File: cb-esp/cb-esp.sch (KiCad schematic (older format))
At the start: 21 parts, among them P1 CONN_01X07, P2 CONN_01X07, P3 CONN_01X02, SW1 SW_PUSH_SMALL, SW2 SW_PUSH_SMALL, U1 MCP1702, U2 ESP-12E, U3 LY-SK10

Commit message: Small changes
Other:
- moved on the sheet: R3
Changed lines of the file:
@@
 L R R3
 U 1 1 5671ECCD
-P 8750 3150
-F 0 "R3" V 8830 3150 50  0000 C CNN
-F 1 "10k" V 8750 3150 50  0000 C CNN
-F 2 "mysmd:SM0603S" H 8750 3150 60  0001 C CNN
-F 3 "" H 8750 3150 60  0001 C CNN
-	1    8750 3150
+P 8800 3300
+F 0 "R3" V 8880 3300 50  0000 C CNN
+F 1 "10k" V 8800 3300 50  0000 C CNN
+F 2 "mysmd:SM0603S" H 8800 3300 60  0001 C CNN
+F 3 "" H 8800 3300 60  0001 C CNN
+	1    8800 3300
 	-1   0    0    1
 $EndComp
 Wire Wire Line
-	8750 2950 8750 3000
+	8800 2950 8800 3150
 $Comp
 L GND #PWR07
 U 1 1 5671ECD5
-P 8750 3350
-F 0 "#PWR07" H 8750 3350 30  0001 C CNN
-F 1 "GND" H 8750 3280 30  0001 C CNN
-F 2 "" H 8750 3350 60  0001 C CNN
-F 3 "" H 8750 3350 60  0001 C CNN
-	1    8750 3350
+P 8800 3500
+F 0 "#PWR07" H 8800 3500 30  0001 C CNN
+F 1 "GND" H 8800 3430 30  0001 C CNN
+F 2 "" H 8800 3500 60  0001 C CNN
+F 3 "" H 8800 3500 60  0001 C CNN
+	1    8800 3500
 	1    0    0    -1
 $EndComp
 Wire Wire Line
-	8750 3300 8750 3350
+	8800 3450 8800 3500
 NoConn ~ 7050 3550
 NoConn ~ 7150 3550
@@
 $EndComp
 Wire Wire Line
-	8750 2950 8200 2950
+	8200 2950 8800 2950
 Wire Wire Line
 	6400 2350 6050 2350

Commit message: Attaching GPIO15 to panStamp's RESET line
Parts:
- PS1: symbol PANSTAMP_NRG2 -> PANSTAMP_NRG2-RESCUE-cb-esp
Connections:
- net PS_RESET is gone; now on net GPIO15: P1.4 (P4), PS1.12 (RESET)
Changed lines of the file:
@@
 EESchema Schematic File Version 2
+LIBS:cb-esp-rescue
 LIBS:power
 LIBS:digi
@@
 Sheet 1 1
 Title "Carrier board for panStamp and ESP-12E"
-Date "2015-12-18"
+Date "2016-02-05"
 Rev "1.0"
 Comp "www.panstamp.com"
@@
 	6850 5400 7300 5400
 Wire Wire Line
-	6850 5300 7300 5300
+	6850 5300 7600 5300
 Wire Wire Line
 	6850 5600 7250 5600
@@
 	6850 5500 6950 5500
 $Comp
-L PANSTAMP_NRG2 PS1
+L PANSTAMP_NRG2-RESCUE-cb-esp PS1
 U 1 1 55D4CB6C
 P 3250 2750
@@
 $EndComp
 Wire Wire Line
-	8350 5200 7900 5200
+	7600 5200 8350 5200
 Text Label 7900 5200 0    60   ~ 0
 GPIO15
@@
 Wire Wire Line
 	8200 2550 9400 2550
+Wire Wire Line
+	7600 5300 7600 5200
 $EndSCHEMATC

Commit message: Version 1.0 released
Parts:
- removed ANT1: ANTENNA, myconnectors:SMA_RightAngle_Tyco, symbol ANTENNA
- removed P1, P2: CONN_01X07, Pin_Headers:Pin_Header_Straight_1x07, symbol CONN_01X07
- removed PS1: PANSTAMP_NRG2, mysmd:PANSTAMP_2, symbol PANSTAMP_NRG2-RESCUE-cb-esp
- removed U3: LY-SK10, mysmd:LY-SK10, symbol LY-SK10
- added D3: D_Schottky_x2_ACom_KKA, mysmd:SOT23, symbol D_Schottky_x2_ACom_KKA
- added D4: BAS16, SOD323, symbol D
- added P1: CONN_01X02, Pin_Headers:Pin_Header_Straight_1x02, symbol CONN_01X02
- added PS1: PANSTAMP_NRG2, mysmd:PANSTAMP_2, symbol PANSTAMP_NRG2
- added PS2: PANSTAMP_MINIBAT, mymods:minibat, symbol PANSTAMP_MINIBAT
- added U3: ANTENNA, myconnectors:SMA_RightAngle_Tyco, symbol ANTENNA
- added U4: LY-SK10, LY-SK10, symbol LY-SK10
- P3: footprint Pin_Headers:Pin_Header_Straight_1x02 -> myconnectors:PWR_3A
- U2: footprint mysmd:ESP-12E -> ESP8266:ESP-12E
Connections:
- net ESP_RXD: now also U4.2
- net ESP_TXD: now also U4.5
- net GND: now also SW1.2, D3.3 (A), P1.2 (P2), PS1.14 (GND), PS1.28 (GND), PS1.29 (GND), PS1.30 (GND), PS1.32 (GND), PS1.33 (GND), PS1.34 (GND), PS2.14 (GND), PS2.16 (GND), U3.2 (GND); no longer SW1.1
- net GPIO0: now also SW1.1; no longer SW1.2
- net GPIO15: now also PS1.12 (RESET), PS2.18 (RESET)
- net PS_RXD: now also PS1.17 (D5/P1.5/UART_RX), PS2.21 (D5/P1.5/UART_RX), U4.6
- net PS_TEST: now also PS1.11 (TEST), PS2.17 (TEST)
- net PS_TXD: now also PS1.16 (D6/P1.6/UART_TX), PS2.20 (D6/P1.6/UART_TX), U4.1
- net VCC: now also PS1.13 (VCC), PS2.15 (VCC)
- net at C1.1, U1.3 (Vin): now also D4.1 (K); no longer P3.1 (P1)
- new net: PS1.31 (ANTENNA), U3.1 (RF)
- new net +5V: D3.1 (K), D3.2 (K), D4.2 (A), P1.1 (P1), P3.1 (P1)
- no-connect marks 36 -> 56
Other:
- moved on the sheet: C1, C2, C3, C4, D1, D2, P3, R1, R2, R3, R4, R5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

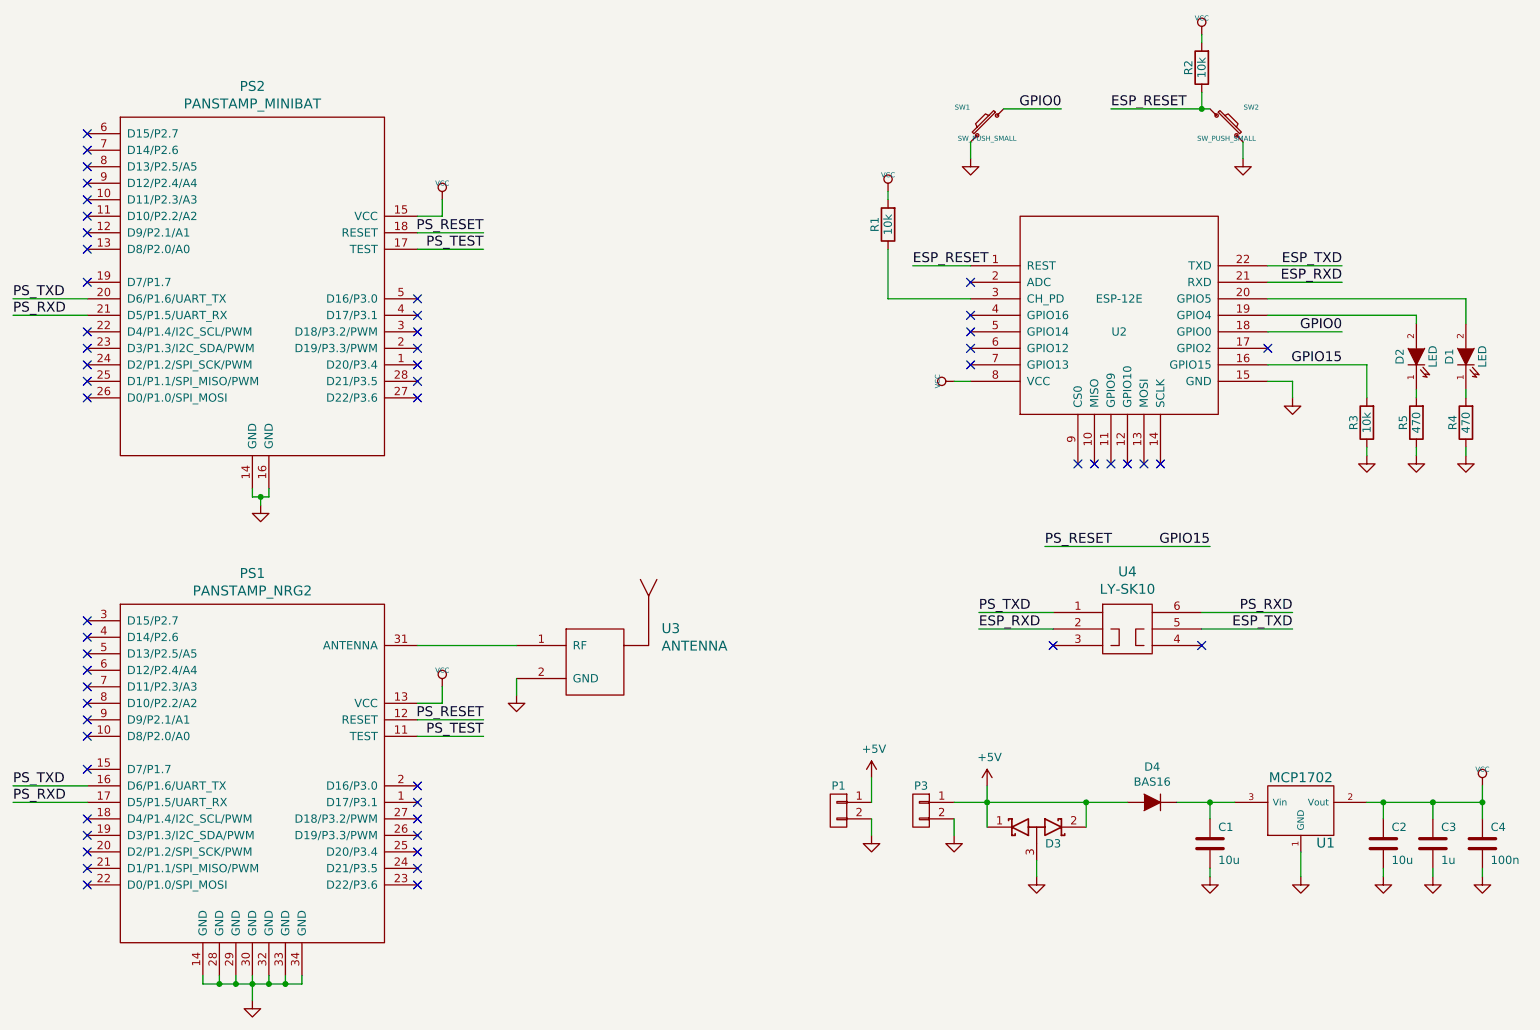
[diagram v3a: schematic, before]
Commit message: New 1.1 version fixing 1.0
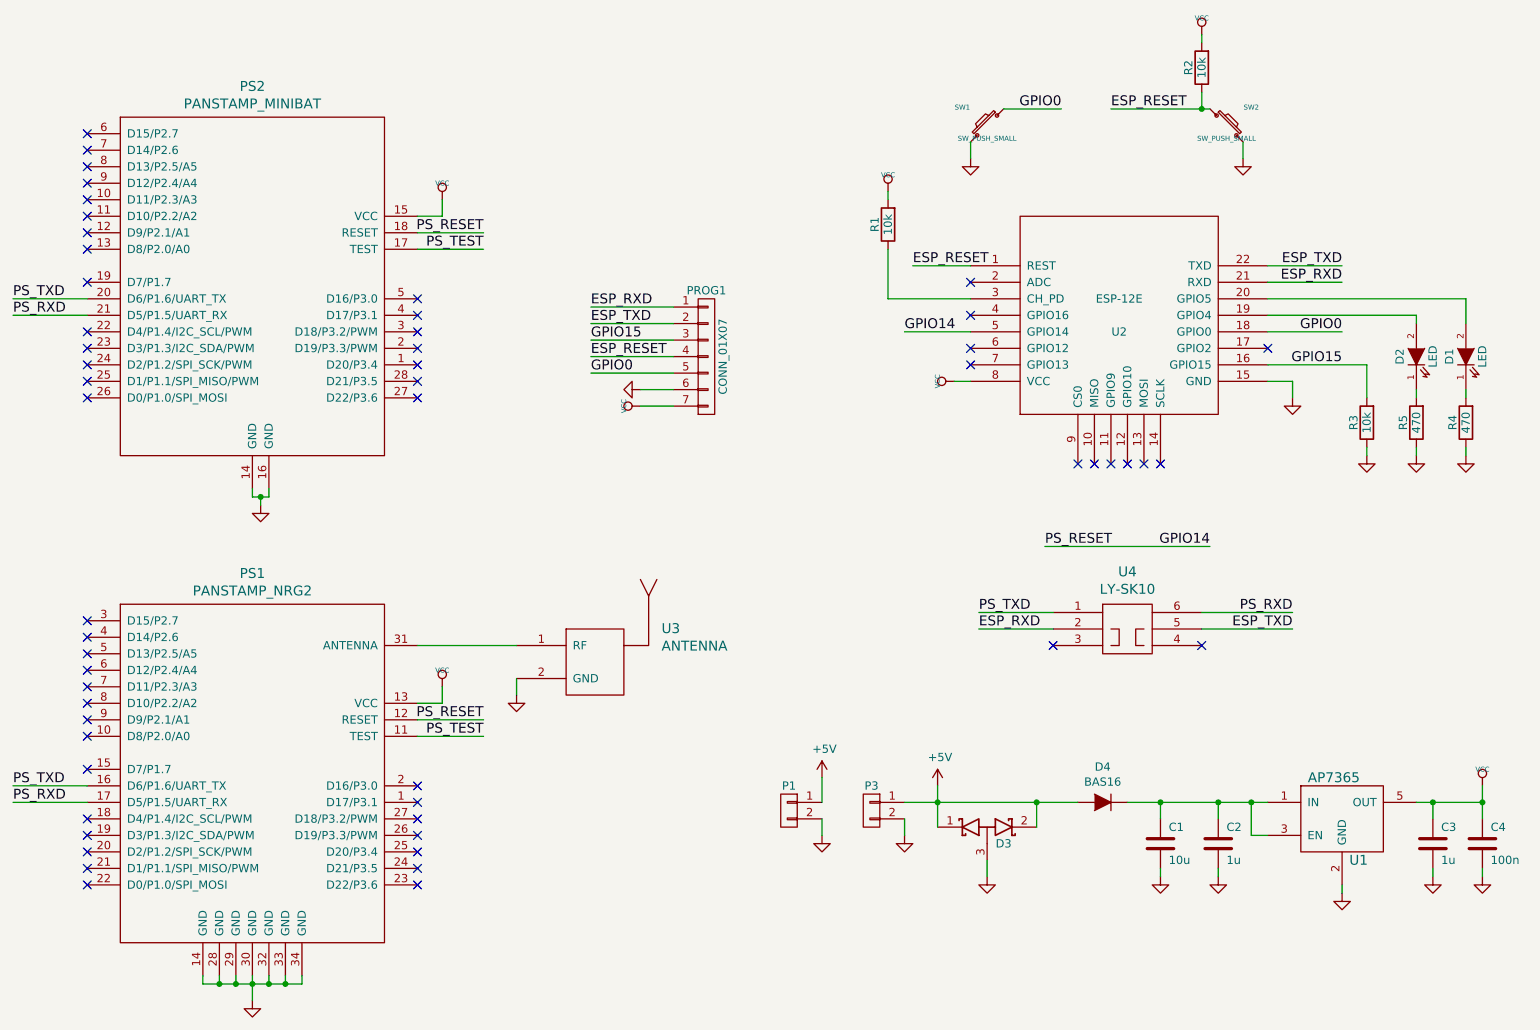
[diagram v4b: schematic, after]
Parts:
- removed U1: MCP1702, libcms:SOT23, symbol MCP1702
- added PROG1: CONN_01X07, Pin_Headers:Pin_Header_Straight_1x07, symbol CONN_01X07
- added U1: AP7365, TO_SOT_Packages_SMD:SOT-23-5, symbol AP7365
- C2: value 10u -> 1u
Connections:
- net ESP_RESET: now also PROG1.4 (P4)
- net ESP_RXD: now also PROG1.1 (P1)
- net ESP_TXD: now also PROG1.2 (P2)
- net GND: now also PROG1.6 (P6), U1.2 (GND)
- net GPIO0: now also PROG1.5 (P5)
- net GPIO15: now also PROG1.3 (P3); no longer PS1.12 (RESET), PS2.18 (RESET)
- net VCC: now also PROG1.7 (P7), U1.5 (OUT); no longer C2.1
- net GPIO14: now reaches U2.5 (GPIO14)
- net GPIO14: now also PS1.12 (RESET), PS2.18 (RESET)
- net at C1.1, D4.1 (K): now also C2.1, U1.1 (IN), U1.3 (EN)
- no-connect marks 56 -> 55
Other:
- moved on the sheet: C1, C2, D3, D4, P1, P3
